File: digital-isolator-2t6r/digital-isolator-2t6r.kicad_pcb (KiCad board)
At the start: 2 copper layers, 47.1 x 42 mm, 28 parts, among them J1 Conn_02x08_Odd_Even, J2 Conn_02x08_Odd_Even, U1 ADuM1401xRW, U2 ADuM1401xRW

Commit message: Added copper tracks to digital iso 2t6r board for in-house fab
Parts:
- added H1: MountingHole, MountingHole:MountingHole_3.2mm_M3, F.Cu at (136.4, 25.9)
- added H2: MountingHole, MountingHole:MountingHole_3.2mm_M3, F.Cu at (136.4, 61.9)
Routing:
- net VDDB: track 79.3 -> 76.7 mm
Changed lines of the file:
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@@
     )
+  )
+  (footprint "MountingHole:MountingHole_3.2mm_M3" (layer "F.Cu")
+    (at 136.42 25.85)
+    (descr "Mounting Hole 3.2mm, no annular, M3")
+    (tags "mounting hole 3.2mm no annular m3")
+    (property "Sheetfile" "digital-isolator-2t6r.kicad_sch")
+    (property "Sheetname" "")
+    (attr exclude_from_pos_files)
+    (fp_text reference "H1" (at 0 -4.2) (layer "F.SilkS")
+      (effects (font (size 1 1) (thickness 0.15)))
+    )
+    (fp_text value "MountingHole" (at 0 4.2) (layer "F.Fab")
+      (effects (font (size 1 1) (thickness 0.15)))
+    )
+    (fp_text user "${REFERENCE}" (at 0 0) (layer "F.Fab")
+      (effects (font (size 1 1) (thickness 0.15)))
+    )
+    (fp_circle (center 0 0) (end 3.2 0) (layer "Cmts.User") (width 0.15) (fill none))
+    (fp_circle (center 0 0) (end 3.45 0) (layer "F.CrtYd") (width 0.05) (fill none))
+    (pad "" np_thru_hole circle (at 0 0) (size 3.2 3.2) (drill 3.2) (layers *.Cu *.Mask))
   )
   (footprint "Resistor_SMD:R_0805_2012Metric_Pad1.20x1.40mm_HandSolder" (layer "F.Cu")
@@
     )
   )
+  (footprint "MountingHole:MountingHole_3.2mm_M3" (layer "F.Cu")
+    (at 136.42 61.85)
+    (descr "Mounting Hole 3.2mm, no annular, M3")
+    (tags "mounting hole 3.2mm no annular m3")
+    (property "Sheetfile" "digital-isolator-2t6r.kicad_sch")
+    (property "Sheetname" "")
+    (attr exclude_from_pos_files)
+    (fp_text reference "H2" (at 0 -4.2) (layer "F.SilkS")
+      (effects (font (size 1 1) (thickness 0.15)))
+    )
+    (fp_text value "MountingHole" (at 0 4.2) (layer "F.Fab")
+      (effects (font (size 1 1) (thickness 0.15)))
+    )
+    (fp_text user "${REFERENCE}" (at 0 0) (layer "F.Fab")
+      (effects (font (size 1 1) (thickness 0.15)))
+    )
+    (fp_circle (center 0 0) (end 3.2 0) (layer "Cmts.User") (width 0.15) (fill none))
+    (fp_circle (center 0 0) (end 3.45 0) (layer "F.CrtYd") (width 0.05) (fill none))
+    (pad "" np_thru_hole circle (at 0 0) (size 3.2 3.2) (drill 3.2) (layers *.Cu *.Mask))
+  )
   (footprint "Package_SO:SOIC-16W_7.5x10.3mm_P1.27mm" (layer "F.Cu")
     (at 114.86 36.09)
@@
     )
   )
+  (gr_line (start 139.45 64.86) (end 92.35 64.86) (layer "F.Cu") (width 0.2))
+  (gr_line (start 92.35 64.86) (end 92.35 22.85) (layer "F.Cu") (width 0.2))
+  (gr_line (start 139.45 22.85) (end 139.45 64.86) (layer "F.Cu") (width 0.2))
+  (gr_line (start 92.35 22.85) (end 139.45 22.85) (layer "F.Cu") (width 0.2))
+  (gr_line (start 139.45 64.86) (end 92.35 64.86) (layer "B.Cu") (width 0.2))
+  (gr_line (start 92.35 22.85) (end 139.45 22.85) (layer "B.Cu") (width 0.2))
+  (gr_line (start 92.35 64.86) (end 92.35 22.85) (layer "B.Cu") (width 0.2))
+  (gr_line (start 139.45 22.85) (end 139.45 64.86) (layer "B.Cu") (width 0.2))
   (gr_rect (start 92.375 22.85) (end 139.425 64.85) (layer "Edge.Cuts") (width 0.1) (fill none))
   (segment (start 132.8 35.475) (end 132.8 31.3) (width 0.3) (layer "F.Cu") (net 1))
@@
   (segment (start 132.8 43.095) (end 128.205 43.095) (width 0.3) (layer "F.Cu") (net 5))
   (segment (start 121.8 58.55) (end 122.75 58.55) (width 0.3) (layer "F.Cu") (net 6))
-  (segment (start 137.1 44.855) (end 137.1 54.7) (width 0.3) (layer "F.Cu") (net 6))
   (segment (start 119.51 57.995) (end 121.245 57.995) (width 0.3) (layer "F.Cu") (net 6))
-  (segment (start 133.25 58.55) (end 122.75 58.55) (width 0.3) (layer "F.Cu") (net 6))
+  (segment (start 137.1 54.7) (end 137.1 44.855) (width 0.3) (layer "F.Cu") (net 6))
+  (segment (start 137.1 44.855) (end 135.34 43.095) (width 0.3) (layer "F.Cu") (net 6))
+  (segment (start 122.75 58.55) (end 133.25 58.55) (width 0.3) (layer "F.Cu") (net 6))
   (segment (start 121.245 57.995) (end 121.8 58.55) (width 0.3) (layer "F.Cu") (net 6))
-  (segment (start 137.1 54.7) (end 133.25 58.55) (width 0.3) (layer "F.Cu") (net 6))
-  (segment (start 135.34 43.095) (end 137.1 44.855) (width 0.3) (layer "F.Cu") (net 6))
+  (segment (start 133.25 58.55) (end 137.1 54.7) (width 0.3) (layer "F.Cu") (net 6))
   (segment (start 125.8 52.2) (end 125.8 48.95) (width 0.3) (layer "F.Cu") (net 7))
   (segment (start 125.8 48.95) (end 129.115 45.635) (width 0.3) (layer "F.Cu") (net 7))
@@
   (via (at 108.25 49.25) (size 1.4) (drill 0.8) (layers "F.Cu" "B.Cu") (net 32))
   (via (at 107.7 41.9) (size 1.4) (drill 0.8) (layers "F.Cu" "B.Cu") (free) (net 32))
+  (segment (start 119.15 27.005) (end 119.135 27.02) (width 0.3) (layer "F.Cu") (net 33))
   (segment (start 119.0875 45.8125) (end 119.0875 46.9) (width 0.3) (layer "F.Cu") (net 33))
-  (segment (start 119.15 25.8) (end 119.15 27.005) (width 0.3) (layer "F.Cu") (net 33))
   (segment (start 119.35 49.5) (end 119.1 49.25) (width 0.3) (layer "F.Cu") (net 33))
-  (segment (start 119.55 25.4) (end 119.15 25.8) (width 0.3) (layer "F.Cu") (net 33))
   (segment (start 119.1225 29.32) (end 119.1225 27.0325) (width 0.3) (layer "F.Cu") (net 33))
   (segment (start 119.35 51.485) (end 119.35 49.5) (width 0.3) (layer "F.Cu") (net 33))
-  (segment (start 119.15 27.005) (end 119.135 27.02) (width 0.3) (layer "F.Cu") (net 33))
+  (segment (start 128.6 25.38) (end 128.58 25.4) (width 0.3) (layer "F.Cu") (net 33))
+  (segment (start 128.58 25.4) (end 119.55 25.4) (width 0.3) (layer "F.Cu") (net 33))
   (segment (start 119.1 49.25) (end 119.1 46.9125) (width 0.3) (layer "F.Cu") (net 33))
   (segment (start 119.51 31.645) (end 119.51 29.7075) (width 0.3) (layer "F.Cu") (net 33))
   (segment (start 119.1225 27.0325) (end 119.135 27.02) (width 0.3) (layer "F.Cu") (net 33))
-  (segment (start 133.75 25.4) (end 119.55 25.4) (width 0.3) (layer "F.Cu") (net 33))
+  (segment (start 119.15 25.8) (end 119.15 27.005) (width 0.3) (layer "F.Cu") (net 33))
   (segment (start 119.51 51.645) (end 119.35 51.485) (width 0.3) (layer "F.Cu") (net 33))
   (segment (start 119.1 46.9125) (end 119.0875 46.9) (width 0.3) (layer "F.Cu") (net 33))
   (segment (start 122.8 44.25) (end 120.65 44.25) (width 0.3) (layer "F.Cu") (net 33))
   (segment (start 120.65 44.25) (end 119.0875 45.8125) (width 0.3) (layer "F.Cu") (net 33))
+  (segment (start 119.55 25.4) (end 119.15 25.8) (width 0.3) (layer "F.Cu") (net 33))
   (segment (start 119.51 29.7075) (end 119.1225 29.32) (width 0.3) (layer "F.Cu") (net 33))
   (via (at 122.8 44.25) (size 1.4) (drill 0.8) (layers "F.Cu" "B.Cu") (net 33))
-  (via (at 133.75 25.4) (size 1.4) (drill 0.8) (layers "F.Cu" "B.Cu") (net 33))
-  (segment (start 137.6 51.5) (end 137.6 29.1) (width 0.3) (layer "B.Cu") (net 33))
-  (segment (start 137.6 29.1) (end 133.9 25.4) (width 0.3) (layer "B.Cu") (net 33))
-  (segment (start 133.9 25.4) (end 133.75 25.4) (width 0.3) (layer "B.Cu") (net 33))
+  (via (at 128.6 25.38) (size 1.4) (drill 0.8) (layers "F.Cu" "B.Cu") (net 33))
+  (segment (start 128.6 25.38) (end 129.42 25.38) (width 0.3) (layer "B.Cu") (net 33))
+  (segment (start 137.6 33.56) (end 137.6 51.5) (width 0.3) (layer "B.Cu") (net 33))
   (segment (start 122.8 44.25) (end 122.961422 44.411422) (width 0.3) (layer "B.Cu") (net 33))
   (segment (start 122.961422 44.411422) (end 137.588578 44.411422) (width 0.3) (layer "B.Cu") (net 33))
-  (segment (start 134.035 51.95) (end 137.15 51.95) (width 0.3) (layer "B.Cu") (net 33))
-  (segment (start 132.8 50.715) (end 134.035 51.95) (width 0.3) (layer "B.Cu") (net 33))
-  (segment (start 137.15 51.95) (end 137.6 51.5) (width 0.3) (layer "B.Cu") (net 33))
+  (segment (start 134.035 51.95) (end 132.8 50.715) (width 0.3) (layer "B.Cu") (net 33))
+  (segment (start 129.42 25.38) (end 137.6 33.56) (width 0.3) (layer "B.Cu") (net 33))
+  (segment (start 137.15 51.95) (end 134.035 51.95) (width 0.3) (layer "B.Cu") (net 33))
+  (segment (start 137.6 51.5) (end 137.15 51.95) (width 0.3) (layer "B.Cu") (net 33))
   (via (at 121.2 29.25) (size 1.4) (drill 0.8) (layers "F.Cu" "B.Cu") (net 34))
   (via (at 121.2 62.75) (size 1.4) (drill 0.8) (layers "F.Cu" "B.Cu") (free) (net 34))

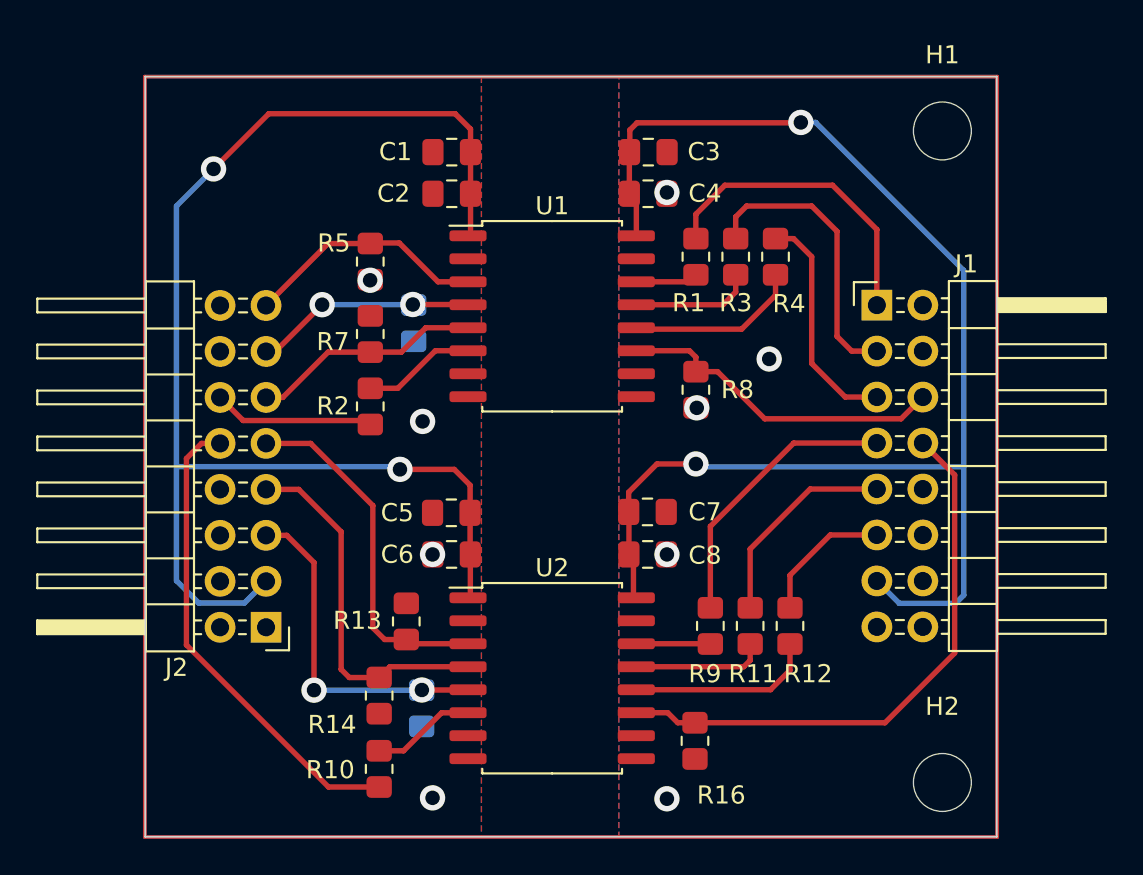
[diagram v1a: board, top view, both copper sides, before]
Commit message: Added pull up resistor to digital isolator 2t6r board
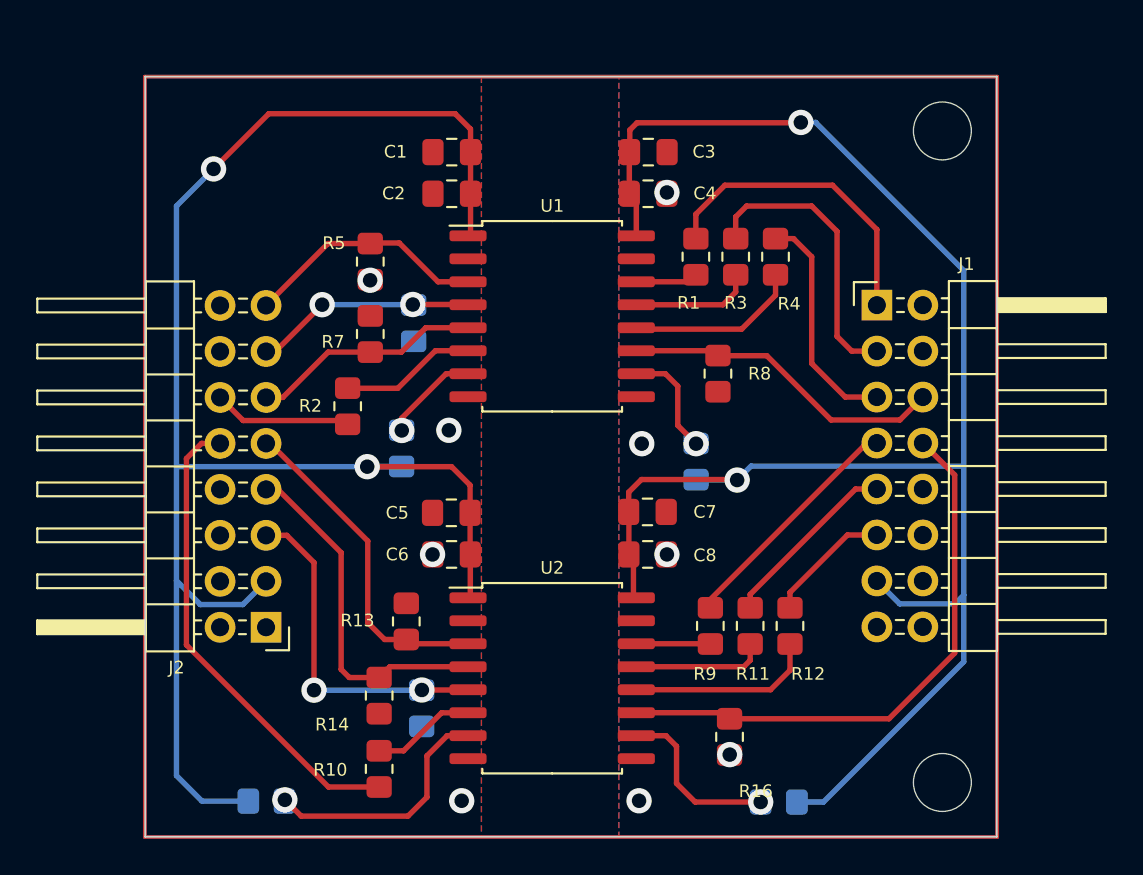
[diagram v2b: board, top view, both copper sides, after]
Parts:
- added R17: 100k, Resistor_SMD:R_0805_2012Metric_Pad1.20x1.40mm_HandSolder, B.Cu at (106.5, 43.4)
- added R18: 100k, Resistor_SMD:R_0805_2012Metric_Pad1.20x1.40mm_HandSolder, B.Cu at (122.8, 44.1)
- added R19: 100k, Resistor_SMD:R_0805_2012Metric_Pad1.20x1.40mm_HandSolder, B.Cu at (99.1, 62.9)
- added R20: 100k, Resistor_SMD:R_0805_2012Metric_Pad1.20x1.40mm_HandSolder, B.Cu at (127.4, 62.9)
- moved R16 1.92 mm to (124.7, 59.3)
- moved R8 1.51 mm to (124.0, 39.3)
- moved R2 1.25 mm to (103.6, 41.1)
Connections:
- U1 pad 10: unconnected-(U1-Pad10) -> Net-(R18-Pad2)
- U1 pad 7: unconnected-(U1-Pad7) -> Net-(R17-Pad1)
- U2 pad 10: unconnected-(U2-Pad10) -> Net-(R20-Pad2)
- U2 pad 7: unconnected-(U2-Pad7) -> Net-(R19-Pad1)
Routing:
- net VDDA: track 74.3 -> 92.8 mm
- net VDDB: track 76.7 -> 95.0 mm
- net Net-(R19-Pad1): track 0.00 -> 13.7 mm, vias 0 -> 1
- net Net-(R20-Pad2): track 0.00 -> 9.59 mm, vias 0 -> 1
- net Net-(R18-Pad2): track 0.00 -> 6.17 mm, vias 0 -> 1
- net Net-(R17-Pad1): track 0.00 -> 5.36 mm, vias 0 -> 1
- net /TX4_B: track 15.6 -> 13.2 mm
- net /TX1_A: track 9.49 -> 7.67 mm
- net /TX5_B: track 11.6 -> 10.2 mm
- net /RX4_A: track 20.2 -> 18.9 mm
- net /adum241x/TX1_A': track 6.26 -> 7.51 mm
- net /RX5_A: track 20.2 -> 19.5 mm
- net /TX6_B: track 7.52 -> 6.97 mm
